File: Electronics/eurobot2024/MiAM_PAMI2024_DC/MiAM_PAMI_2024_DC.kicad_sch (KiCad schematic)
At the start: 30 parts, among them J1 Conn_01x03_Male, J2 Conn_01x03_Male, J3 SSD1306_vertical, Q1 BS170F, SW1 SW_DPDT_x2, U1 ESP32-DEVKITC-32U, U2 3V3, U4 5V, U6 TB6612FNG

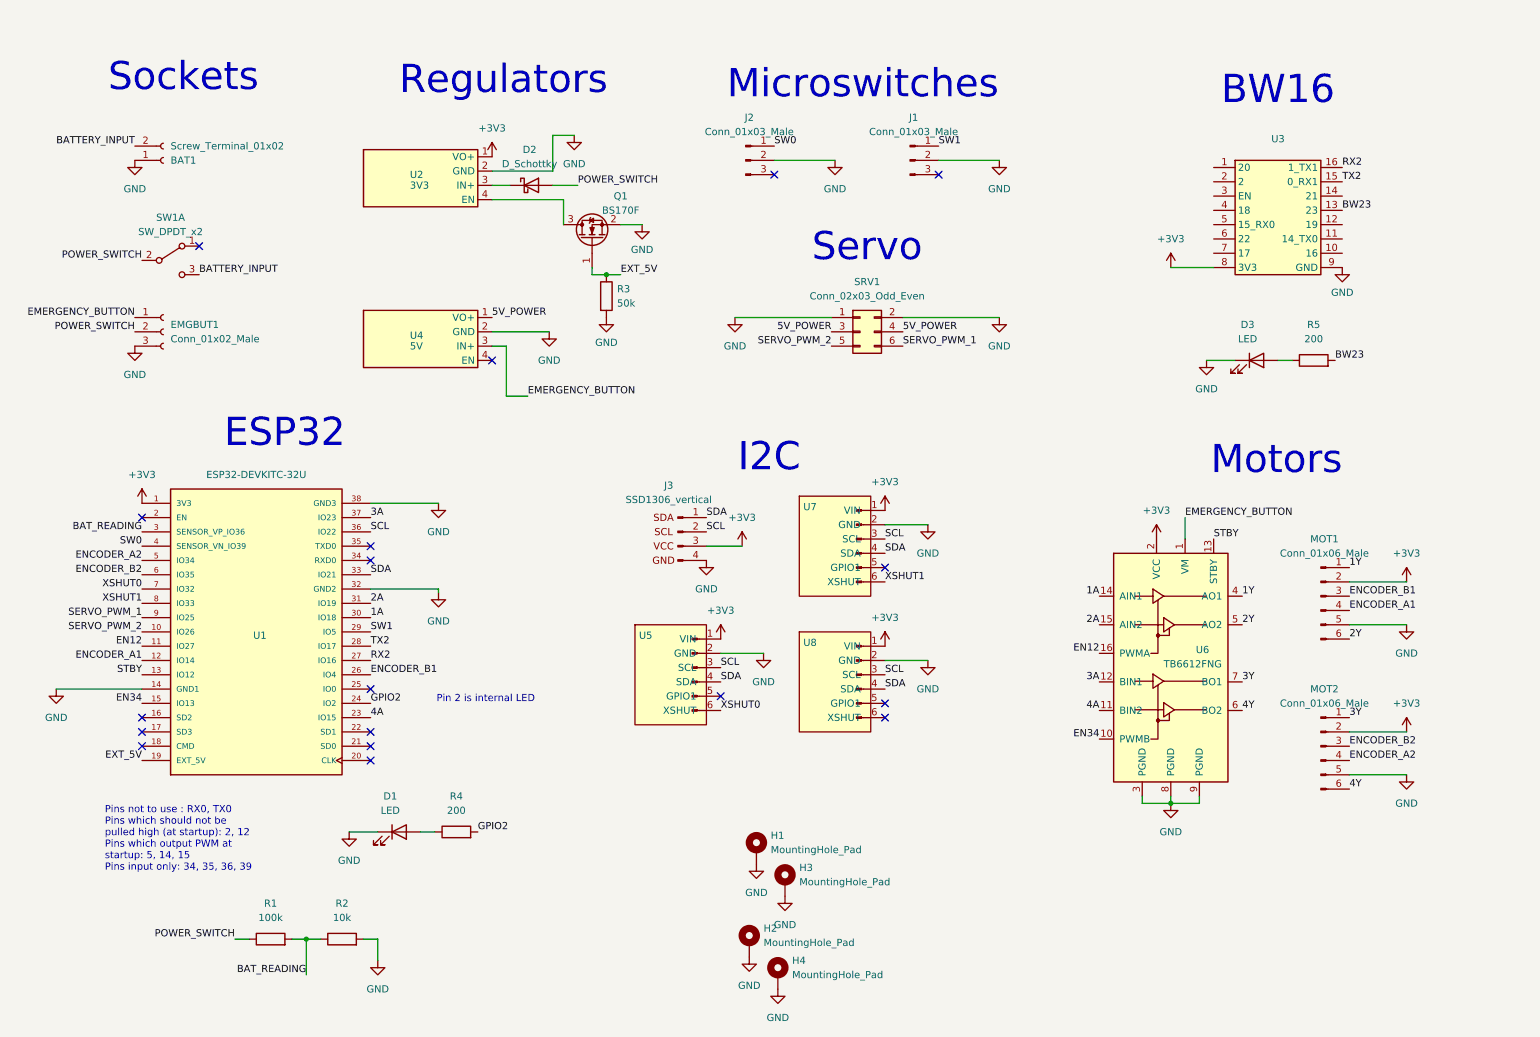
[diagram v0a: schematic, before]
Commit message: Add new PAMI PCB
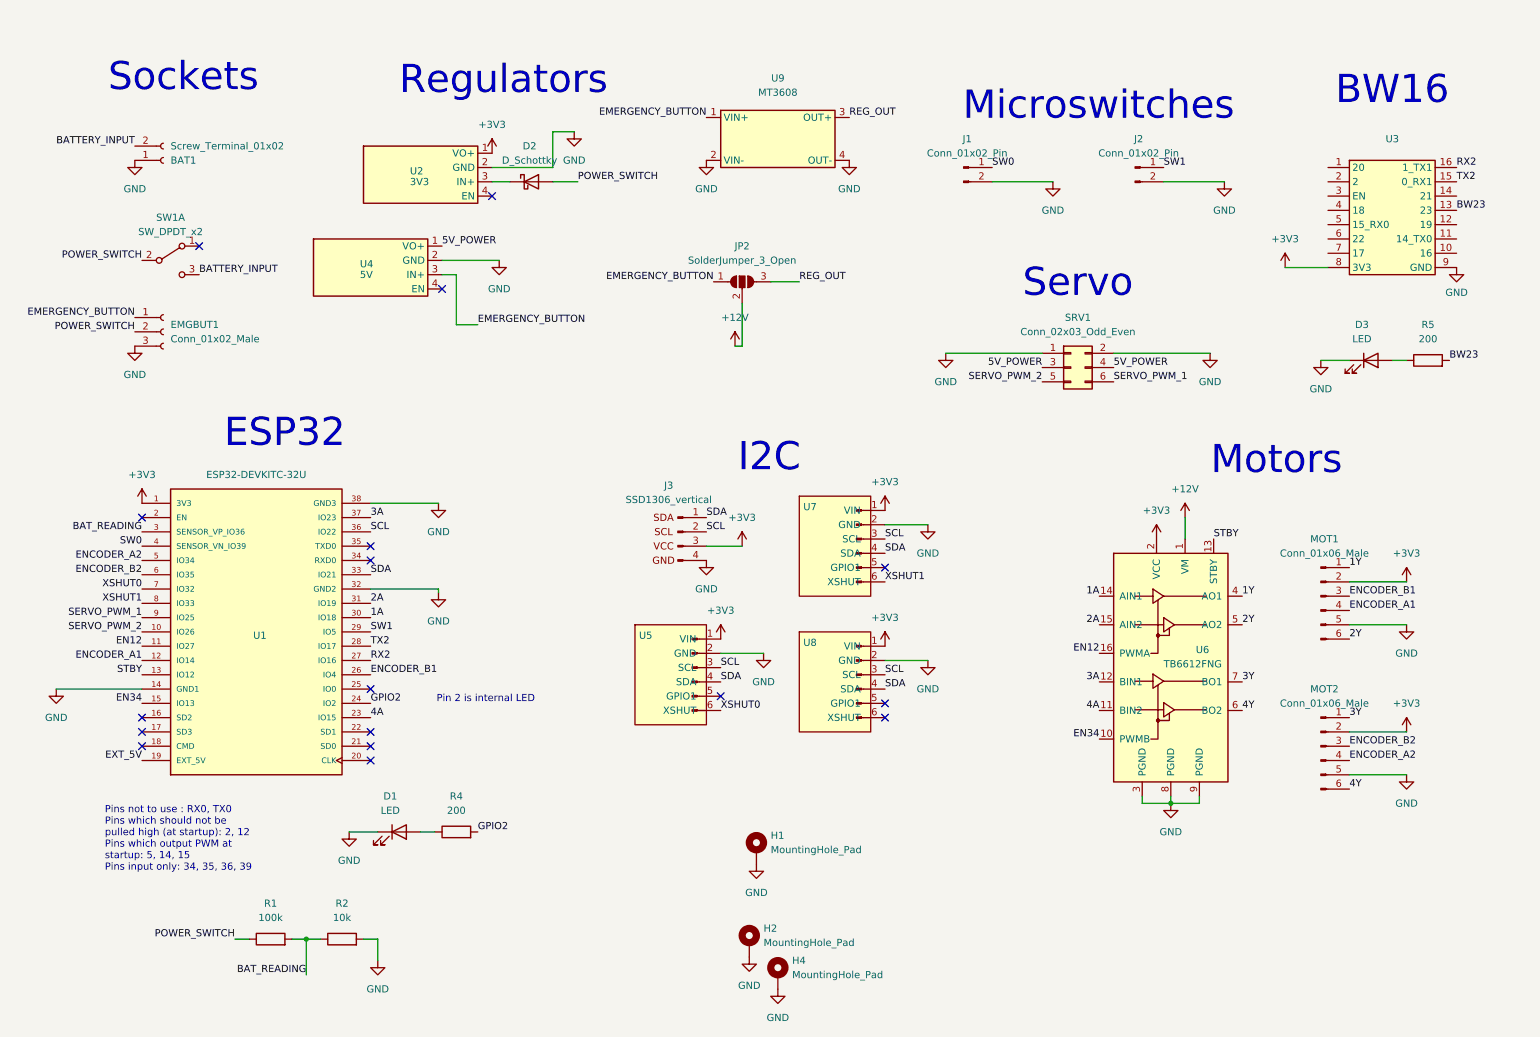
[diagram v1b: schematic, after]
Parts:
- removed H3: MountingHole_Pad, MountingHole:MountingHole_3.2mm_M3_DIN965_Pad, symbol Mechanical:MountingHole_Pad
- removed J1, J2: Conn_01x03_Male, MiAM_ESP32_Footprints:Microruptor, symbol Connector:Conn_01x03_Male
- removed Q1: BS170F, Package_TO_SOT_SMD:SOT-23, symbol Transistor_FET:BS170F
- removed R3: 50k, Resistor_SMD:R_0805_2012Metric, symbol Device:R
- added J1, J2: Conn_01x02_Pin, Connector_PinHeader_2.54mm:PinHeader_1x02_P2.54mm_Vertical, symbol Connector:Conn_01x02_Pin
- added JP2: SolderJumper_3_Open, Connector_PinHeader_2.54mm:PinHeader_1x03_P2.54mm_Vertical, symbol Jumper:SolderJumper_3_Open
- added U9: MT3608, MiAM_ESP32_Footprints:MT3608, symbol MiAM_ESP32:MT3608
- J3: footprint MiAM_ESP32_Footprints:SSD1306_vertical -> Connector_PinHeader_2.54mm:PinHeader_1x04_P2.54mm_Vertical
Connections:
- net EMERGENCY_BUTTON: now also JP2.1 (A), U9.1 (VIN+); no longer U6.1 (VM)
- net GND: now also J1.2 (Pin_2), J2.2 (Pin_2), U9.2 (VIN-), U9.4 (OUT-)
- net SW0: now also J1.1 (Pin_1)
- net SW1: now also J2.1 (Pin_1)
- new net +12V: JP2.2 (C), U6.1 (VM)
- new net REG_OUT: JP2.3 (B), U9.3 (OUT+)
- no-connect marks 18 -> 17
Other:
- moved on the sheet: D2, D3, R5, SRV1, U2, U3, U4

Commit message: Add LED ring and better routing
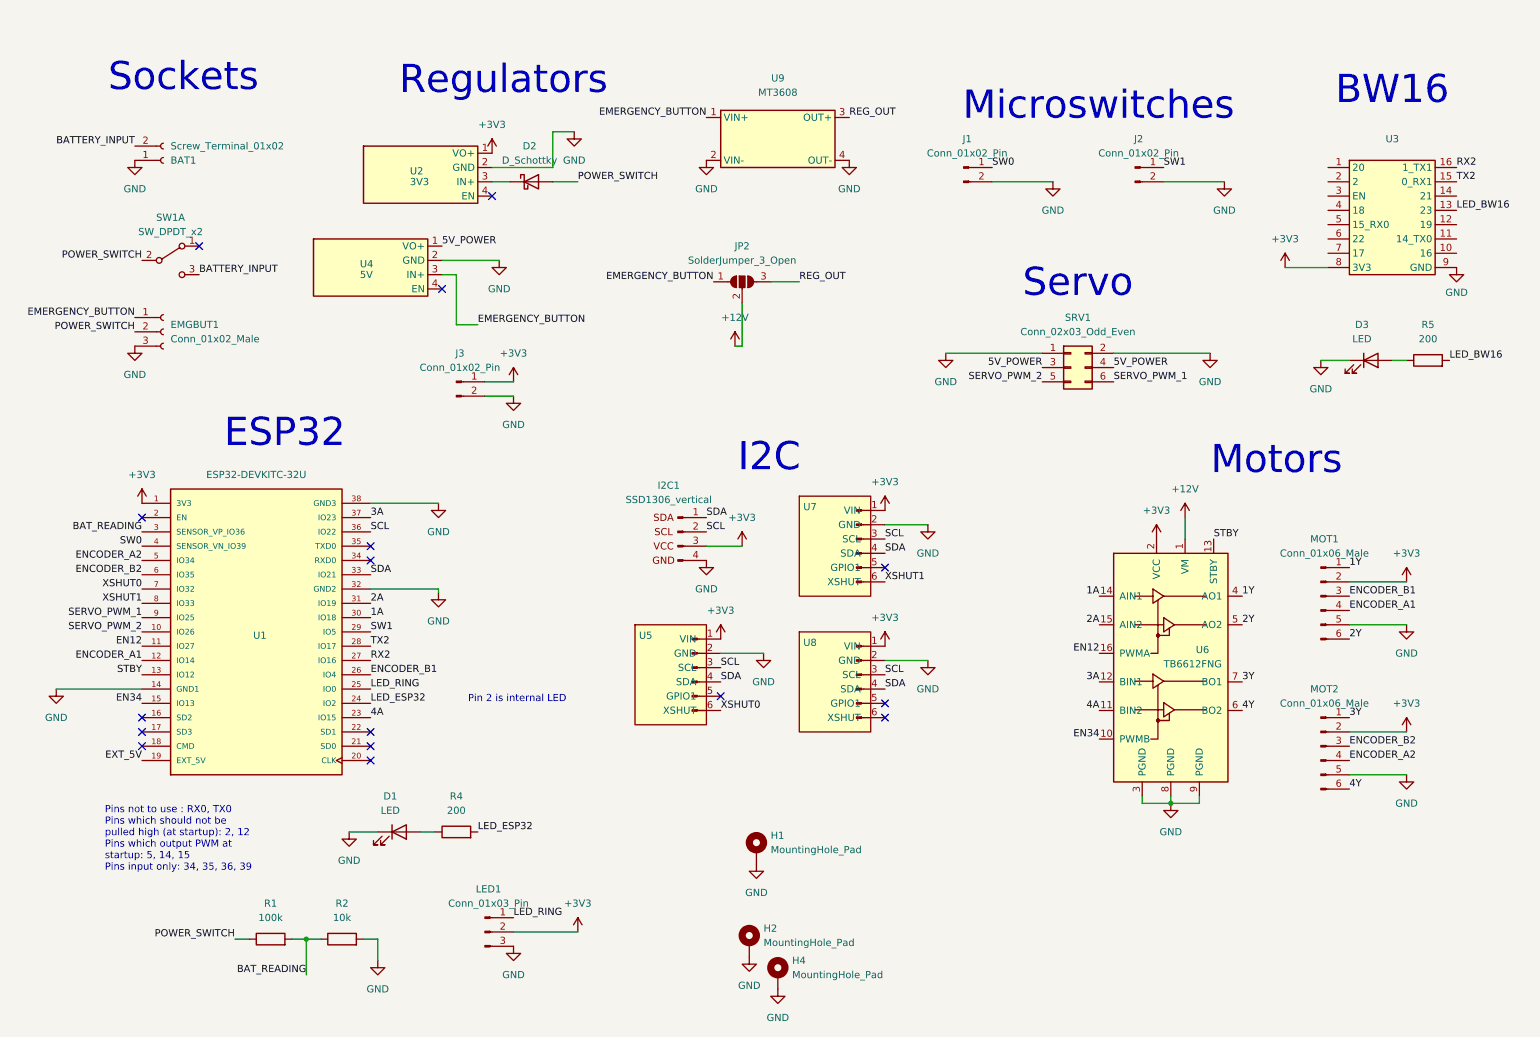
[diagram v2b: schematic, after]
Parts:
- added J3: Conn_01x02_Pin, Connector_PinHeader_2.54mm:PinHeader_1x02_P2.54mm_Vertical, symbol Connector:Conn_01x02_Pin
- added LED1: Conn_01x03_Pin, Connector_PinHeader_2.54mm:PinHeader_1x03_P2.54mm_Vertical, symbol Connector:Conn_01x03_Pin
- renumbered J3 to I2C1
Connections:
- net +3V3: now also J3.1 (Pin_1), LED1.2 (Pin_2)
- net GND: now also J3.2 (Pin_2), LED1.3 (Pin_3)
- net LED_RING: now reaches U1.25 (IO0)
- net LED_RING: now also LED1.1 (Pin_1)
- net BW23 renamed LED_BW16
- net GPIO2 renamed LED_ESP32
- no-connect marks 17 -> 16

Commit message: Fix PAMI pcb
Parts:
- D1, D3: footprint LED_THT:LED_D3.0mm -> LED_SMD:LED_0805_2012Metric
- JP2: footprint Connector_PinHeader_2.54mm:PinHeader_1x03_P2.54mm_Vertical -> Jumper:SolderJumper-3_P1.3mm_Bridged12_Pad1.0x1.5mm_NumberLabels
- R4: value 200 -> 1K
- R5: value 200 -> 5K
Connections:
- net +3V3: now also LED1.1 (Pin_1); no longer LED1.2 (Pin_2)
- net LED_RING: now also LED1.2 (Pin_2); no longer LED1.1 (Pin_1)
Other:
- moved on the sheet: H1
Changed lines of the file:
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@@
 	(wire
 		(pts
-			(xy 219.71 43.18) (xy 230.505 43.18)
+			(xy 104.14 173.99) (xy 115.57 173.99)
 		)
 		(stroke
@@
 	(wire
 		(pts
-			(xy 226.06 153.67) (xy 226.06 152.4)
+			(xy 219.71 43.18) (xy 230.505 43.18)
 		)
 		(stroke
@@
 	(wire
 		(pts
-			(xy 247.65 74.93) (xy 252.73 74.93)
+			(xy 226.06 153.67) (xy 226.06 152.4)
 		)
 		(stroke
@@
 	(wire
 		(pts
-			(xy 111.125 43.18) (xy 115.57 43.18)
+			(xy 247.65 74.93) (xy 252.73 74.93)
 		)
 		(stroke
@@
 	(wire
 		(pts
-			(xy 180.975 73.66) (xy 198.12 73.66)
+			(xy 111.125 43.18) (xy 115.57 43.18)
 		)
 		(stroke
@@
 	(wire
 		(pts
-			(xy 93.98 68.58) (xy 97.79 68.58)
+			(xy 180.975 73.66) (xy 198.12 73.66)
 		)
 		(stroke
@@
 	(wire
 		(pts
-			(xy 104.14 176.53) (xy 115.57 176.53)
+			(xy 93.98 68.58) (xy 97.79 68.58)
 		)
 		(stroke
@@
 		)
 	)
+	(label "LED_RING"
+		(at 104.14 176.53 0)
+		(fields_autoplaced yes)
+		(effects
+			(font
+				(size 1.27 1.27)
+			)
+			(justify left bottom)
+		)
+	)
 	(label "STBY"
 		(at 228.6 106.68 0)
@@
 		)
 	)
-	(label "LED_RING"
-		(at 104.14 173.99 0)
-		(fields_autoplaced yes)
-		(effects
-			(font
-				(size 1.27 1.27)
-			)
-			(justify left bottom)
-		)
-	)
 	(label "SDA"
 		(at 78.74 113.03 0)
@@
 	)
 	(symbol
+		(lib_id "miam_logo:LOGO")
+		(at 137.16 162.56 0)
+		(unit 1)
+		(exclude_from_sim no)
+		(in_bom yes)
+		(on_board yes)
+		(dnp no)
+		(fields_autoplaced yes)
+		(property "Reference" "#G1"
+			(at 137.16 113.3263 0)
+			(effects
+				(font
+					(size 1.27 1.27)
+				)
+				(hide yes)
+			)
+		)
+		(property "Value" "LOGO"
+			(at 137.16 211.7937 0)
+			(effects
+				(font
+					(size 1.27 1.27)
+				)
+				(hide yes)
+			)
+		)
+		(property "Footprint" "MiAM_ESP32_Footprints:miam_logo"
+			(at 137.16 162.56 0)
+			(effects
+				(font
+					(size 1.27 1.27)
+				)
+				(hide yes)
+			)
+		)
+		(property "Datasheet" ""
+			(at 137.16 162.56 0)
+			(effects
+				(font
+					(size 1.27 1.27)
+				)
+				(hide yes)
+			)
+		)
+		(property "Description" ""
+			(at 137.16 162.56 0)
+			(effects
+				(font
+					(size 1.27 1.27)
+				)
+				(hide yes)
+			)
+		)
+		(instances
+			(project ""
+				(path "/25619b26-f8ce-486a-87c9-e743f43b219f"
+					(reference "#G1")
+					(unit 1)
+				)
+			)
+		)
+	)
+	(symbol
 		(lib_id "power:GND")
 		(at 146.05 180.975 0)
@@
 			)
 		)
-		(property "Value" "200"
+		(property "Value" "5K"
 			(at 266.7 71.12 90)
 			(effects
@@
 			)
 		)
-		(property "Description" ""
+		(property "Description" "Green"
 			(at 266.7 74.93 0)
 			(effects
@@
 	(symbol
 		(lib_id "power:GND")
-		(at 147.32 164.465 0)
+		(at 154.94 170.18 0)
 		(unit 1)
 		(exclude_from_sim no)
@@
 		(fields_autoplaced yes)
 		(property "Reference" "#PWR012"
-			(at 147.32 170.815 0)
+			(at 154.94 176.53 0)
 			(effects
 				(font
@@
 		)
 		(property "Value" "GND"
-			(at 147.32 169.545 0)
+			(at 154.94 175.26 0)
 			(effects
 				(font
@@
 		)
 		(property "Footprint" ""
-			(at 147.32 164.465 0)
+			(at 154.94 170.18 0)
 			(effects
 				(font
@@
 		)
 		(property "Datasheet" ""
-			(at 147.32 164.465 0)
+			(at 154.94 170.18 0)
 			(effects
 				(font
@@
 		)
 		(property "Description" ""
-			(at 147.32 164.465 0)
+			(at 154.94 170.18 0)
 			(effects
 				(font
@@
 			)
 		)
-		(property "Footprint" "LED_THT:LED_D3.0mm"
+		(property "Footprint" "LED_SMD:LED_0805_2012Metric"
 			(at 83.82 158.75 0)
 			(effects
@@
 			)
 		)
-		(property "Footprint" "LED_THT:LED_D3.0mm"
+		(property "Footprint" "LED_SMD:LED_0805_2012Metric"
 			(at 256.54 74.93 0)
 			(effects
@@
 	(symbol
 		(lib_id "power:+3V3")
-		(at 115.57 176.53 0)
+		(at 115.57 173.99 0)
 		(mirror y)
 		(unit 1)
@@
 		(dnp no)
 		(property "Reference" "#PWR037"
-			(at 115.57 180.34 0)
+			(at 115.57 177.8 0)
 			(effects
 				(font
@@
 		)
 		(property "Value" "+3V3"
-			(at 115.57 171.45 0)
+			(at 115.57 168.91 0)
 			(effects
 				(font
@@
 		)
 		(property "Footprint" ""
-			(at 115.57 176.53 0)
+			(at 115.57 173.99 0)
 			(effects
 				(font
@@
 		)
 		(property "Datasheet" ""
-			(at 115.57 176.53 0)
+			(at 115.57 173.99 0)
 			(effects
 				(font
@@
 		)
 		(property "Description" ""
-			(at 115.57 176.53 0)
+			(at 115.57 173.99 0)
 			(effects
 				(font
@@
 			)
 		)
-		(property "Footprint" "Connector_PinHeader_2.54mm:PinHeader_1x03_P2.54mm_Vertical"
+		(property "Footprint" "Jumper:SolderJumper-3_P1.3mm_Bridged12_Pad1.0x1.5mm_NumberLabels"
 			(at 144.78 60.96 0)
 			(effects
@@
 			)
 		)
-		(property "Value" "200"
+		(property "Value" "1K"
 			(at 93.98 154.94 90)
 			(effects
@@
 			)
 		)
-		(property "Description" ""
+		(property "Description" "Red"
 			(at 93.98 158.75 0)
 			(effects
@@
 	(symbol
 		(lib_id "Mechanical:MountingHole_Pad")
-		(at 147.32 161.925 0)
+		(at 154.94 167.64 0)
 		(unit 1)
 		(exclude_from_sim no)
@@
 		(fields_autoplaced yes)
 		(property "Reference" "H1"
-			(at 149.86 159.385 0)
+			(at 157.48 165.1 0)
 			(effects
 				(font
@@
 		)
 		(property "Value" "MountingHole_Pad"
-			(at 149.86 161.925 0)
+			(at 157.48 167.64 0)
 			(effects
 				(font
@@
 		)
 		(property "Footprint" "MountingHole:MountingHole_3.2mm_M3_DIN965_Pad"
-			(at 147.32 161.925 0)
+			(at 154.94 167.64 0)
 			(effects
 				(font
@@
 		)
 		(property "Datasheet" "~"
-			(at 147.32 161.925 0)
+			(at 154.94 167.64 0)
 			(effects
 				(font
@@
 		)
 		(property "Description" ""
-			(at 147.32 161.925 0)
+			(at 154.94 167.64 0)
 			(effects
 				(font
